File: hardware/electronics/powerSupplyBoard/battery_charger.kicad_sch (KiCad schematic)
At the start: 37 parts, among them J5 Barrel_Jack_Switch, J6 S2B-PH-SM4-TB, J7 PREC002SAAN-RC, J8 PREC003SAAN-RC, Q1 BUK961R6, U4 BQ25798

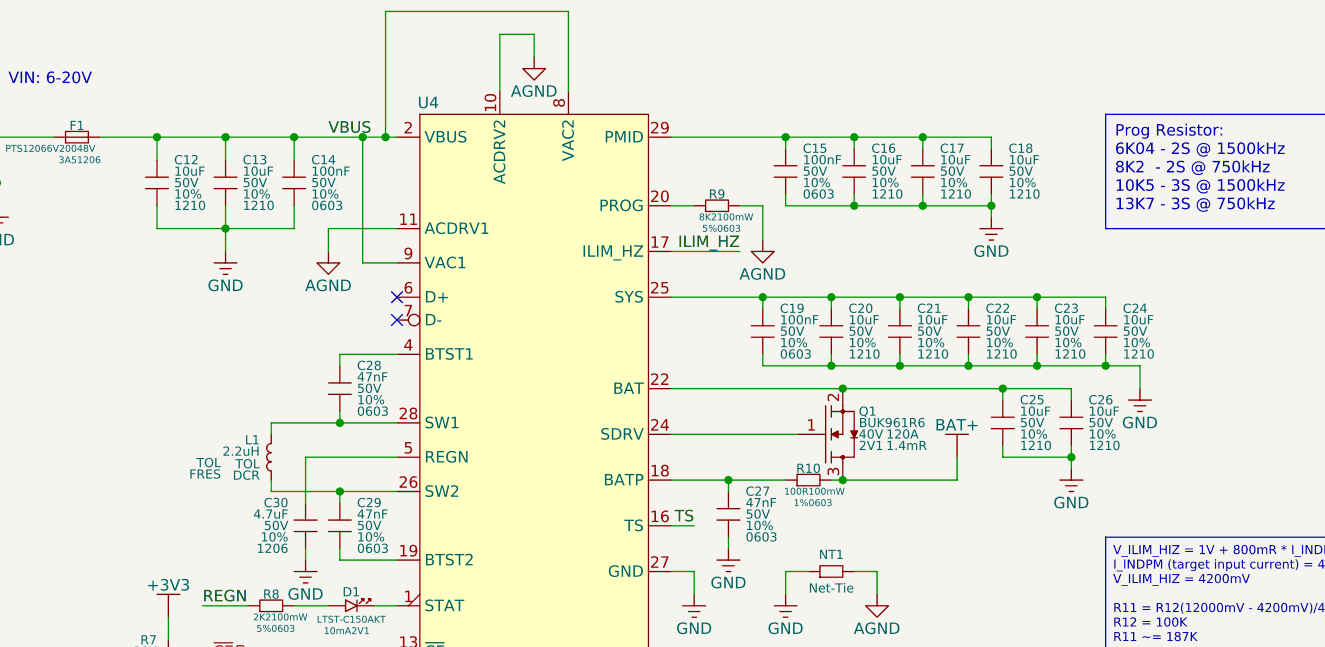
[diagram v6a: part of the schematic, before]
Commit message: replaced old 1210 10uF capacitors with 1206 ones
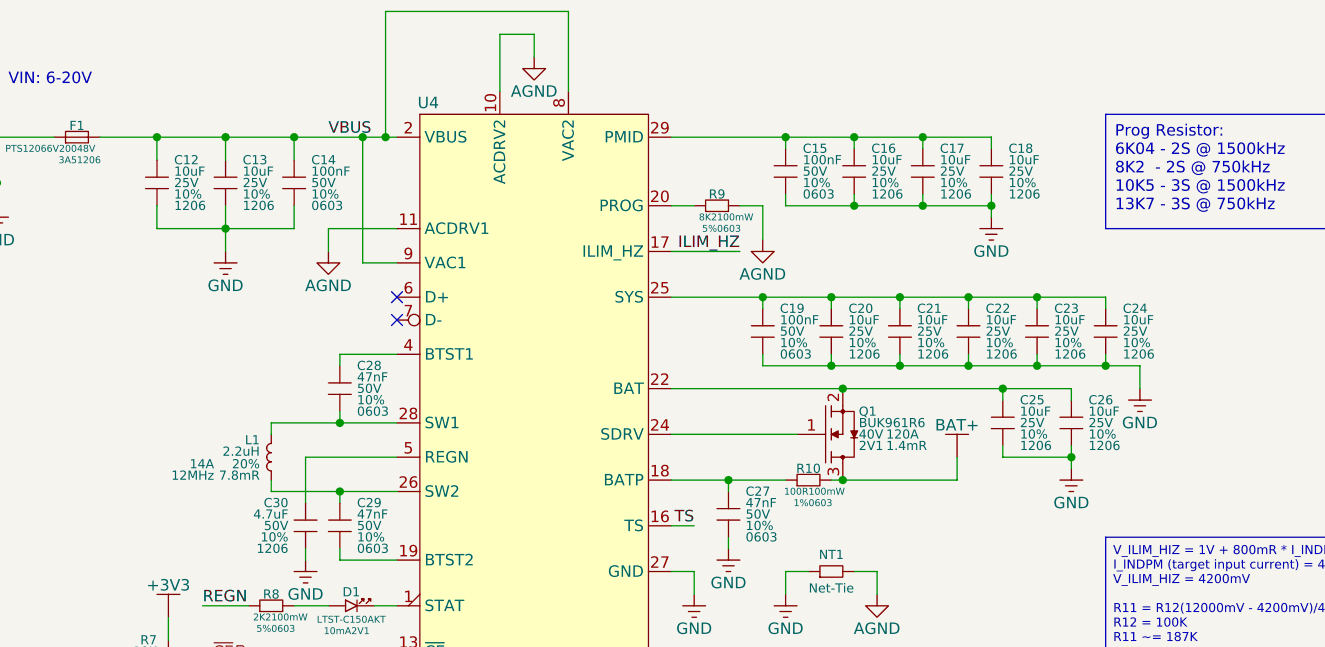
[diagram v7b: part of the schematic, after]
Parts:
- C12, C13, C16, C17, C18, C20, C21, C22, C23, C24, C25, C26: footprint lib_fp:MLCC1210 -> lib_fp:MLCC1206; DKPN 478-KAM32LR71H106KUCT-ND -> 445-CGA5L1X7R1E106K160DCCT-ND; MPN KAM32LR71H106KU -> CGA5L1X7R1E106K160DC; Manufacturer KYOCERA AVX -> TDK Corporation; Package 1210 -> 1206; Voltage Rating 50V -> 25V
- L1: footprint lib_fp:HCM1A1105V2 -> lib_fp:EXLA1V06; Current Rating TOL -> 14A; DC Resistance DCR -> 7.8mR; DKPN 283-HCM1A1105V2-2R2-RCT-ND -> 283-EXLA1V0606-2R2-RCT-ND; MPN HCM1A1105V2-2R2-R -> EXLA1V0606-2R2-R; Resonant Frequency FRES -> 12MHz; Tolerance TOL -> 20%

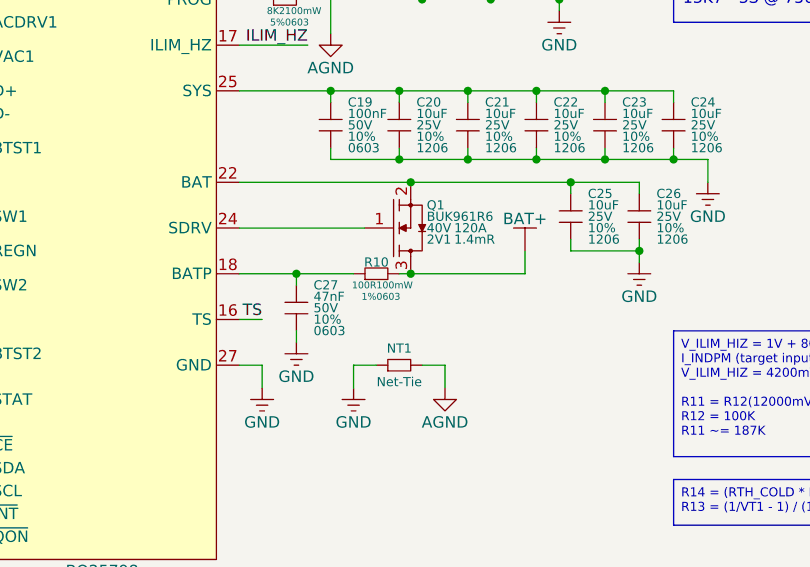
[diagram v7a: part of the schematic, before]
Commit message: replaced batt charger PMOS
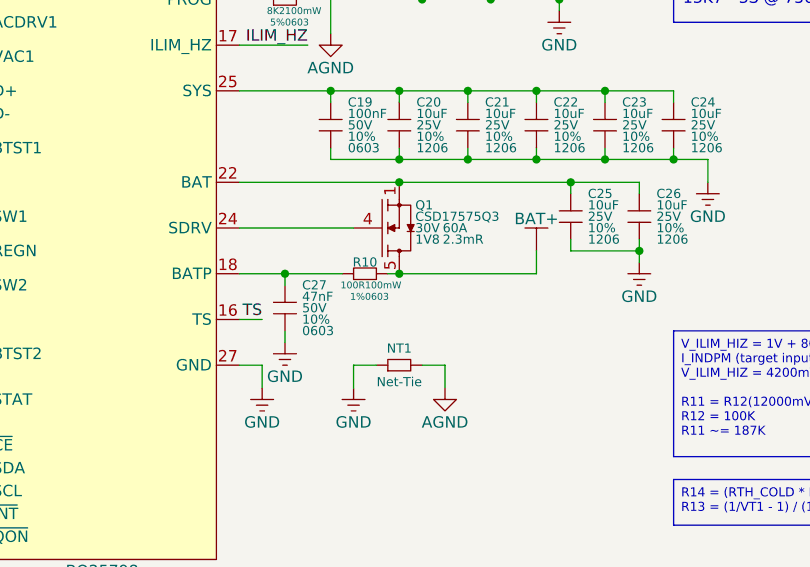
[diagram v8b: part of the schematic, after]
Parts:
- removed Q1: BUK961R6, lib_fp:SOT404, symbol lib_sch:NMOS_GSD_1
- added Q1: CSD17575Q3, lib_fp:SON8P65_330X330X100L45X34N, symbol lib_sch:NMOS_SGD_PWR
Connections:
- net BAT+: now also Q1.5, Q1.6, Q1.7, Q1.8
- net at C25.1, C26.1, U4.22 (BAT)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: now also Q1.1, Q1.2, Q1.3
- net at U4.24 (SDRV): now also Q1.4
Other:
- moved on the sheet: C27, R10
